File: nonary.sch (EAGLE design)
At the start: 47 parts, among them J1 USB-C-12401598E4#2A, K1 KEYSWITCH-LEDTHTHOLE-MXHS-1U-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, K10 KEYSWITCH-LEDTHTHOLE-MXHS-1U-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, K11 KEYSWITCH-LEDTHTHOLE-MXHS-1U-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, K12 KEYSWITCH-LEDTHTHOLE-MXHS-1U-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, K13 KEYSWITCH-LEDTHTHOLE-MXHS-1U-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, K14 KEYSWITCH-LEDTHTHOLE-MXHS-1U-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, K15 KEYSWITCH-LEDTHTHOLE-MXHS-1U-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, K16 KEYSWITCH-LEDTHTHOLE-MXHS-1U-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, K2 KEYSWITCH-LEDTHTHOLE-MXHS-1U-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, K3 KEYSWITCH-LEDTHTHOLE-MXHS-1U-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, K4 KEYSWITCH-LEDTHTHOLE-MXHS-1U-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, K5 KEYSWITCH-LEDTHTHOLE-MXHS-1U-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, K6 KEYSWITCH-LEDTHTHOLE-MXHS-1U-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, K7 KEYSWITCH-LEDTHTHOLE-MXHS-1U-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, K8 KEYSWITCH-LEDTHTHOLE-MXHS-1U-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, K9 KEYSWITCH-LEDTHTHOLE-MXHS-1U-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

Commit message: updated file names
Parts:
- removed K1, K10, K11, K12, K13, K14, K15, K16, K2, K3, K4, K5, K6, K7, K8, K9: KEYSWITCH-LEDTHTHOLE-MXHS-1U-LEDTHTHOLE, Keyboard:KEYSWITCH-LEDTHTHOLE-MXHS-1U-LEDTHTHOLE
- added D15, D16, D17, D18, D19, D20, D21, D22, D23, D24, D25, D26, D28, D29, D30, D31, D32, D33, D34, D35, D36, D37, D38, D39, D40, D41, D42, D43, D44, D45, D46, D47, D48, D49, D50, D51, D52, D53, D54, D55, D56, D57, D58, D59, D60, D61, D62: (no value), Components:DIODE-DFN0603-2
- added F1, F2, F3, F4, F5, K_", K_,, K_-, K_., K_/, K_0, K_1, K_2, K_3, K_4, K_5, K_6, K_7, K_8, K_9, K_=, K_A, K_B, K_BACKSLASH, K_BACKSPACE, K_C, K_CAPSLOCK, K_D, K_E, K_ENTER, K_F, K_G, K_H, K_I, K_J, K_K, K_L, K_LALT, K_LCTRL, K_LSHIFT, K_LWIN, K_M, K_N, K_O, K_P, K_Q, K_R, K_RALT, K_RCTRL, K_RFN1, K_RFN2, K_RSHIFT, K_RWIN, K_S, K_SEMICOLON, K_SPACE, K_T, K_TAB, K_U, K_V, K_W, K_X, K_Y, K_Z, K_[, K_], K_`: KEYSWITCH-LEDTHTHOLE-MXHS-1U-LEDTHTHOLE, Keyboard:KEYSWITCH-LEDTHTHOLE-MXHS-1U-LEDTHTHOLE
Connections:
- new net COL10: K_..P0, K_9.P0, K_L.P0, K_O.P0, K_RALT.P0
- new net COL12: K_/.P0, K_0.P0, K_P.P0, K_RWIN.P0, K_SEMICOLON.P0
- new net COL13: K_".P0, K_-.P0, K_RFN2.P0, K_RSHIFT.P0, K_[.P0
- new net COL14: K_BACKSLASH.P0, K_BACKSPACE.P0, K_ENTER.P0, K_RCTRL.P0, K_RFN1.P0
- new net COL2: K_1.P0, K_A.P0, K_LWIN.P0, K_Q.P0, K_Z.P0
- new net COL3: K_2.P0, K_LALT.P0, K_S.P0, K_W.P0, K_X.P0
- new net COL4: K_3.P0, K_C.P0, K_D.P0, K_E.P0
- new net COL5: K_4.P0, K_F.P0, K_R.P0, K_V.P0
- new net COL6: K_5.P0, K_B.P0, K_G.P0, K_SPACE.P0, K_T.P0
- new net COL7: K_6.P0, K_H.P0, K_N.P0, K_Y.P0
- new net COL8: K_7.P0, K_J.P0, K_M.P0, K_U.P0
- new net COL9: K_,.P0, K_8.P0, K_I.P0, K_K.P0
- new net N$19: D10.A, D9.C, K_8.P1
- new net N$25: D14.C, K_BACKSPACE.P1
- new net N$26: D15.C, D16.A, K_TAB.P1
- new net N$27: D16.C, D17.A, K_Q.P1
- new net N$28: D17.C, D18.A, K_W.P1
- new net N$29: D18.C, D19.A, K_E.P1
- new net N$30: D19.C, D20.A, K_R.P1
- new net N$31: D20.C, D21.A, K_T.P1
- new net N$32: D21.C, D22.A, K_Y.P1
- new net N$33: D22.C, D23.A, K_U.P1
- new net N$34: D23.C, D24.A, K_I.P1
- new net N$35: D24.C, D25.A, K_O.P1
- new net N$36: D25.C, D26.A, K_P.P1
- new net N$37: D26.C, D27.A, K_[.P1
- new net N$38: D34.C, D35.A, K_G.P1
- new net N$39: D27.C, D28.A, K_].P1
- new net N$40: D41.C, K_ENTER.P1
- new net N$41: D29.C, D30.A, K_CAPSLOCK.P1
- new net N$42: D30.C, D31.A, K_A.P1
- new net N$43: D31.C, D32.A, K_S.P1
- new net N$44: D32.C, D33.A, K_D.P1
- new net N$45: D33.C, D34.A, K_F.P1
- new net N$46: D40.C, D41.A, K_".P1
- new net N$47: D35.C, D36.A, K_H.P1
- new net N$48: D36.C, D37.A, K_J.P1
- new net N$49: D37.C, D38.A, K_K.P1
- new net N$50: D38.C, D39.A, K_L.P1
- new net N$51: D39.C, D40.A, K_SEMICOLON.P1
- new net N$52: D53.C, D54.A, K_RSHIFT.P1
- new net N$53: D54.C, K_RFN1.P1
- new net N$54: D47.C, D48.A, K_B.P1
- new net N$55: D60.C, D61.A, K_RWIN.P1
- new net N$56: D42.C, D43.A, K_LSHIFT.P1
- new net N$57: D43.C, D44.A, K_Z.P1
- new net N$58: D44.C, D45.A, K_X.P1
- new net N$59: D45.C, D46.A, K_C.P1
- new net N$60: D46.C, D47.A, K_V.P1
- new net N$61: K_=.P0, K_].P0
- new net N$62: D48.C, D49.A, K_N.P1
- new net N$63: D49.C, D50.A, K_M.P1
- new net N$64: D50.C, D51.A, K_,.P1
- new net N$65: D51.C, D52.A, K_..P1
- new net N$66: D52.C, D53.A, K_/.P1
- new net N$71: D55.C, D56.A, K_LCTRL.P1
- new net N$72: D56.C, D57.A, K_LWIN.P1
- new net N$73: D57.C, D58.A, K_LALT.P1
- new net N$74: D58.C, D59.A, K_SPACE.P1
- new net N$75: D59.C, D60.A, K_RALT.P1
- new net N$77: D61.C, D62.A, K_RFN2.P1
- new net N$78: D62.C, K_RCTRL.P1
- new net ROW1: D15.A, F2.P1, U$1.PF1(ADC1)
- new net ROW3: D42.A, F4.P1, U$1.PF5(ADC5)
- new net ROW4: D55.A, F5.P1, U$1.PF6(ADC6)
- net COL0: now also F1.P0, F2.P0, F3.P0, F4.P0, F5.P0, U$1.PF7(ADC7); no longer K1.P0, K15.P0, K16.P0, U$1.PF4(ADC4)
- net COL1: now also K_CAPSLOCK.P0, K_LCTRL.P0, K_LSHIFT.P0, K_TAB.P0, K_`.P0; no longer U$1.PF5(ADC5)
- net N$11: now also D1.C, D2.A, K_`.P1; no longer D2.C, D3.A, K3.P1
- net N$12: now also D2.C, D3.A, K_1.P1; no longer D3.C, D4.A, K4.P1
- net N$13: now also D3.C, D4.A, K_2.P1; no longer D1.C, D2.A, K2.P1
- net N$14: now also K_3.P1; no longer K5.P1
- net N$15: now also K_4.P1; no longer K6.P1
- net N$16: now also K_5.P1; no longer K7.P1
- net N$17: now also K_6.P1; no longer K8.P1
- net N$18: now also K_7.P1; no longer K9.P1
- net N$20: now also D10.C, D11.A, K_9.P1; no longer D10.A, D9.C, K10.P1
- net N$21: now also D11.C, D12.A, K_0.P1; no longer D10.C, D11.A, K11.P1
- net N$22: now also D12.C, D13.A, K_-.P1; no longer D11.C, D12.A, K12.P1
- net N$23: now also D28.C, K_BACKSLASH.P1; no longer D12.C, D13.A, K13.P1
- net N$24: now also D14.A, K_=.P1; no longer K14.P1
- net N$7: now also R3.1; no longer R3.2
- net N$8: now also R3.2; no longer R3.1
- net ROW0: now also F1.P1; no longer K1.P1
- net ROW2: now also D29.A, F3.P1, U$1.PF4(ADC4); no longer D14.A, D27.A, K15.P1, K16.P1, U$1.PF1(ADC1)
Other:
- note added: "Fn Keys"
- note removed: "Power"
- moved on the sheet: C1, C2, C3, C4, C5, C6, C7, C8, D1, D10, D11, D12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

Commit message: Made modifications to the keyboard.lbr, brd, and sch files
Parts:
- removed D1, D10, D11, D12, D13, D14, D15, D16, D17, D18, D19, D2, D20, D21, D22, D23, D24, D25, D26, D27, D28, D29, D3, D30, D31, D32, D33, D34, D35, D36, D37, D38, D39, D4, D40, D41, D42, D43, D44, D45, D46, D47, D48, D49, D5, D50, D51, D52, D53, D54, D55, D56, D57, D58, D59, D6, D60, D61, D62, D8, D9: (no value), Components:DIODE-DFN0603-2
- removed F1, F3, F4, F5, K_", K_,, K_-, K_., K_/, K_0, K_1, K_2, K_3, K_4, K_5, K_6, K_7, K_8, K_9, K_=, K_A, K_B, K_BACKSLASH, K_BACKSPACE, K_C, K_CAPSLOCK, K_D, K_E, K_ENTER, K_F, K_G, K_H, K_I, K_J, K_K, K_L, K_LALT, K_LCTRL, K_LSHIFT, K_LWIN, K_M, K_N, K_O, K_P, K_Q, K_R, K_RALT, K_RCTRL, K_RFN1, K_RFN2, K_RSHIFT, K_RWIN, K_S, K_SEMICOLON, K_SPACE, K_T, K_TAB, K_U, K_V, K_W, K_X, K_Y, K_Z, K_[, K_], K_`: KEYSWITCH-LEDTHTHOLE-MXHS-1U-LEDTHTHOLE, Keyboard:KEYSWITCH-LEDTHTHOLE-MXHS-1U-LEDTHTHOLE
- removed J1: USB-C-12401598E4#2A, USB:USB-C-12401598E4#2A
- removed R4: 22, rcl:R-US_R0603
- added C10, C11, C9: 0.1uF, Components:CAPACITOR-0603
- added C12, C13, C14: 0.47uF, Components:CAPACITOR-0603
- added IC1: IS31FL3733-TQLS4, SamacSys_Parts:IS31FL3733-TQLS4
- added IC2: TLV75533PDBVR, SamacSys_Parts:TLV75533PDBVR
- added J2: USB4065-XX-X_REVA, USB4065-XX-X_REVA:USB4065-XX-X_REVA
- added K1, K2, K3, K4, K5, K6, K7, K8, K9: KEYSWITCH-RGBSMDLED-MXHSPCB-1U-SMDRGB, Keyboard:KEYSWITCH-RGBSMDLED-MXHSPCB-1U-SMDRGB
- added Q1, Q2: BSS138, SamacSys_Parts:BSS138
- added R10, R11, R8, R9: 10K, rcl:R-US_R0603
- added R5, R6: 5.1k, rcl:R-US_R0603
- added SV1: (no value), con-lstb:MA04-1
- C8: value 22pF -> 1uF
- D7: value (none) -> PRTR5V0U2X,215; device Components:DIODE-DFN0603-2 -> SamacSys_Parts:PRTR5V0U2X,215
- F2: value KEYSWITCH-LEDTHTHOLE-MXHS-1U-LEDTHTHOLE -> MF-PSMF020X-2; device Keyboard:KEYSWITCH-LEDTHTHOLE-MXHS-1U-LEDTHTHOLE -> SamacSys_Parts:MF-PSMF020X-2
- R3: value 22 -> 10K
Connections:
- net N$1 renamed XTAL1
- net N$2 renamed XTAL2
- removed net COL0: F1.P0, F2.P0, F3.P0, F4.P0, F5.P0, U$1.PF7(ADC7)
- removed net COL1: K_CAPSLOCK.P0, K_LCTRL.P0, K_LSHIFT.P0, K_TAB.P0, K_`.P0
- removed net COL10: K_..P0, K_9.P0, K_L.P0, K_O.P0, K_RALT.P0
- removed net COL12: K_/.P0, K_0.P0, K_P.P0, K_RWIN.P0, K_SEMICOLON.P0
- removed net COL13: K_".P0, K_-.P0, K_RFN2.P0, K_RSHIFT.P0, K_[.P0
- removed net COL14: K_BACKSLASH.P0, K_BACKSPACE.P0, K_ENTER.P0, K_RCTRL.P0, K_RFN1.P0
- removed net COL2: K_1.P0, K_A.P0, K_LWIN.P0, K_Q.P0, K_Z.P0
- removed net COL3: K_2.P0, K_LALT.P0, K_S.P0, K_W.P0, K_X.P0
- removed net COL4: K_3.P0, K_C.P0, K_D.P0, K_E.P0
- removed net COL5: K_4.P0, K_F.P0, K_R.P0, K_V.P0
- removed net COL6: K_5.P0, K_B.P0, K_G.P0, K_SPACE.P0, K_T.P0
- removed net COL7: K_6.P0, K_H.P0, K_N.P0, K_Y.P0
- removed net COL8: K_7.P0, K_J.P0, K_M.P0, K_U.P0
- removed net COL9: K_,.P0, K_8.P0, K_I.P0, K_K.P0
- removed net N$10: J1.D_M, R4.2
- removed net N$11: D1.C, D2.A, K_`.P1
- removed net N$12: D2.C, D3.A, K_1.P1
- removed net N$14: D4.C, D5.A, K_3.P1
- removed net N$15: D5.C, D6.A, K_4.P1
- removed net N$16: D6.C, D7.A, K_5.P1
- removed net N$17: D7.C, D8.A, K_6.P1
- removed net N$18: D8.C, D9.A, K_7.P1
- removed net N$20: D10.C, D11.A, K_9.P1
- removed net N$21: D11.C, D12.A, K_0.P1
- removed net N$22: D12.C, D13.A, K_-.P1
- removed net N$23: D28.C, K_BACKSLASH.P1
- removed net N$24: D13.C, D14.A, K_=.P1
- removed net N$25: D14.C, K_BACKSPACE.P1
- removed net N$28: D17.C, D18.A, K_W.P1
- removed net N$29: D18.C, D19.A, K_E.P1
- removed net N$30: D19.C, D20.A, K_R.P1
- removed net N$31: D20.C, D21.A, K_T.P1
- removed net N$32: D21.C, D22.A, K_Y.P1
- removed net N$33: D22.C, D23.A, K_U.P1
- removed net N$34: D23.C, D24.A, K_I.P1
- removed net N$35: D24.C, D25.A, K_O.P1
- removed net N$36: D25.C, D26.A, K_P.P1
- removed net N$37: D26.C, D27.A, K_[.P1
- removed net N$38: D34.C, D35.A, K_G.P1
- removed net N$39: D27.C, D28.A, K_].P1
- removed net N$40: D41.C, K_ENTER.P1
- removed net N$41: D29.C, D30.A, K_CAPSLOCK.P1
- removed net N$42: D30.C, D31.A, K_A.P1
- removed net N$43: D31.C, D32.A, K_S.P1
- removed net N$44: D32.C, D33.A, K_D.P1
- removed net N$45: D33.C, D34.A, K_F.P1
- removed net N$46: D40.C, D41.A, K_".P1
- removed net N$47: D35.C, D36.A, K_H.P1
- removed net N$48: D36.C, D37.A, K_J.P1
- removed net N$49: D37.C, D38.A, K_K.P1
- removed net N$50: D38.C, D39.A, K_L.P1
- removed net N$51: D39.C, D40.A, K_SEMICOLON.P1
- removed net N$52: D53.C, D54.A, K_RSHIFT.P1
- removed net N$53: D54.C, K_RFN1.P1
- removed net N$54: D47.C, D48.A, K_B.P1
- removed net N$55: D60.C, D61.A, K_RWIN.P1
- removed net N$56: D42.C, D43.A, K_LSHIFT.P1
- removed net N$57: D43.C, D44.A, K_Z.P1
- removed net N$58: D44.C, D45.A, K_X.P1
- removed net N$59: D45.C, D46.A, K_C.P1
- removed net N$6: J1.VCC, U$1.UVCC
- removed net N$60: D46.C, D47.A, K_V.P1
- removed net N$61: K_=.P0, K_].P0
- removed net N$62: D48.C, D49.A, K_N.P1
- removed net N$63: D49.C, D50.A, K_M.P1
- removed net N$64: D50.C, D51.A, K_,.P1
- removed net N$65: D51.C, D52.A, K_..P1
- removed net N$66: D52.C, D53.A, K_/.P1
- removed net N$7: J1.D_P, R3.1
- removed net N$71: D55.C, D56.A, K_LCTRL.P1
- removed net N$72: D56.C, D57.A, K_LWIN.P1
- removed net N$73: D57.C, D58.A, K_LALT.P1
- removed net N$74: D58.C, D59.A, K_SPACE.P1
- removed net N$75: D59.C, D60.A, K_RALT.P1
- removed net N$77: D61.C, D62.A, K_RFN2.P1
- removed net N$78: D62.C, K_RCTRL.P1
- removed net N$8: R3.2, U$1.D+
- removed net N$9: R4.1, U$1.D-
- removed net ROW0: D1.A, F1.P1, U$1.PF0(ADC0)
- removed net ROW1: D15.A, F2.P1, U$1.PF1(ADC1)
- removed net ROW2: D29.A, F3.P1, U$1.PF4(ADC4)
- removed net ROW3: D42.A, F4.P1, U$1.PF5(ADC5)
- removed net ROW4: D55.A, F5.P1, U$1.PF6(ADC6)
- removed net VCC: C3.2, C4.2, C5.2, C6.2, C7.2, U$1.AVCC@24, U$1.AVCC@44, U$1.VBUS, U$1.VCC@14, U$1.VCC@34
- new net +5V: C3.2, C4.2, C5.2, C6.2, C7.2, F2.1, IC2.EN, IC2.IN, R1.1, R10.1, R8.1, SV1.3, U$1.AVCC@24, U$1.AVCC@44, U$1.UVCC, U$1.VBUS, U$1.VCC@14, U$1.VCC@34
- new net AVCC: C12.2, C9.2, IC1.AVCC, IC1.DVCC
- new net CS1: IC1.CS3, K3.LED+, K6.LED+, K9.LED+
- new net CS2: IC1.CS2, K2.LED+, K5.LED+, K8.LED+
- new net CS3: IC1.CS1, K1.LED+, K4.LED+, K7.LED+
- new net D+: D7.I/O_1, J2.DP1, J2.DP2, U$1.D+
- new net D-: D7.I/O_2, J2.DN1, J2.DN2, U$1.D-
- new net KEY1: K1.P0, U$1.PD7(ADC10)
- new net KEY2: K2.P0, U$1.PF5(ADC5)
- new net KEY3: K3.P0, U$1.PF0(ADC0)
- new net KEY4: K4.P0, U$1.PD6(ADC9)
- new net KEY5: K5.P0, U$1.PF6(ADC6)
- new net KEY6: K6.P0, U$1.PF1(ADC1)
- new net KEY7: K7.P0, U$1.PD4(ADC8)
- new net KEY8: K8.P0, U$1.PF7(ADC7)
- new net KEY9: K9.P0, U$1.PF4(ADC4)
- new net PVCC_1: C11.2, C14.2, IC1.PVCC_1
- new net PVCC_2: C10.2, C13.2, IC1.PVCC_2
- new net SCL: Q2.D, R10.2, U$1.PD0(SCL)
- new net SCL_3V3: IC1.SCL, Q2.S, R11.2, SV1.2
- new net SDA: Q1.D, R8.2, U$1.PD1(SDA)
- new net SDA_3V3: IC1.SDA, Q1.S, R9.2, SV1.1
- new net SW1: IC1.SW1, K1.B-, K2.B-, K3.B-
- new net SW2: IC1.SW2, K1.G-, K2.G-, K3.G-
- new net SW3: IC1.SW3, K1.R-, K2.R-, K3.R-
- new net SW4: IC1.SW4, K4.B-, K5.B-, K6.B-
- new net SW5: IC1.SW5, K4.G-, K5.G-, K6.G-
- new net SW6: IC1.SW6, K4.R-, K5.R-, K6.R-
- new net SW7: IC1.SW7, K7.B-, K8.B-, K9.B-
- new net SW8: IC1.SW8, K7.G-, K8.G-, K9.G-
- new net SW9: IC1.SW9, K7.R-, K8.R-, K9.R-
- net +3V3: now also IC1.VIO, IC2.OUT, Q1.G, Q2.G, R11.1, R9.1; no longer R1.1
- net GND: now also C10.1, C11.1, C12.1, C13.1, C14.1, C9.1, D7.GND, IC1.ADDR1, IC1.ADDR2, IC1.AGND, IC1.GND_1, IC1.GND_2, IC1.PGND_1, IC1.PGND_2, IC2.GND, IC2.NC, J2.GND1.1, J2.GND1.2, J2.GND2.1, J2.GND2.2, J2.SHIELD, K1.P1, K2.P1, K3.P1, K4.P1, K5.P1, K6.P1, K7.P1, K8.P1, K9.P1, R3.2, R5.2, R6.2, SV1.4; no longer J1.GND, J1.SHIELD
- net N$13: now also J2.CC2, R5.1; no longer D3.C, D4.A, K_2.P1
- net N$19: now also J2.CC1, R6.1; no longer D10.A, D9.C, K_8.P1
- net N$26: now also IC1.RSET, R3.1; no longer D15.C, D16.A, K_TAB.P1
- net N$27: now also D7.VCC, F2.2, J2.VBUS1.1, J2.VBUS2.2; no longer D16.C, D17.A, K_Q.P1
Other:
- note added: "Switch Matrix"
- note added: "USB Type-C"
- note removed: "Fn Keys"
- note removed: "USB"
- moved on the sheet: C1, C2, C3, C4, C5, C6, C7, C8, R1, R2, R3, S1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

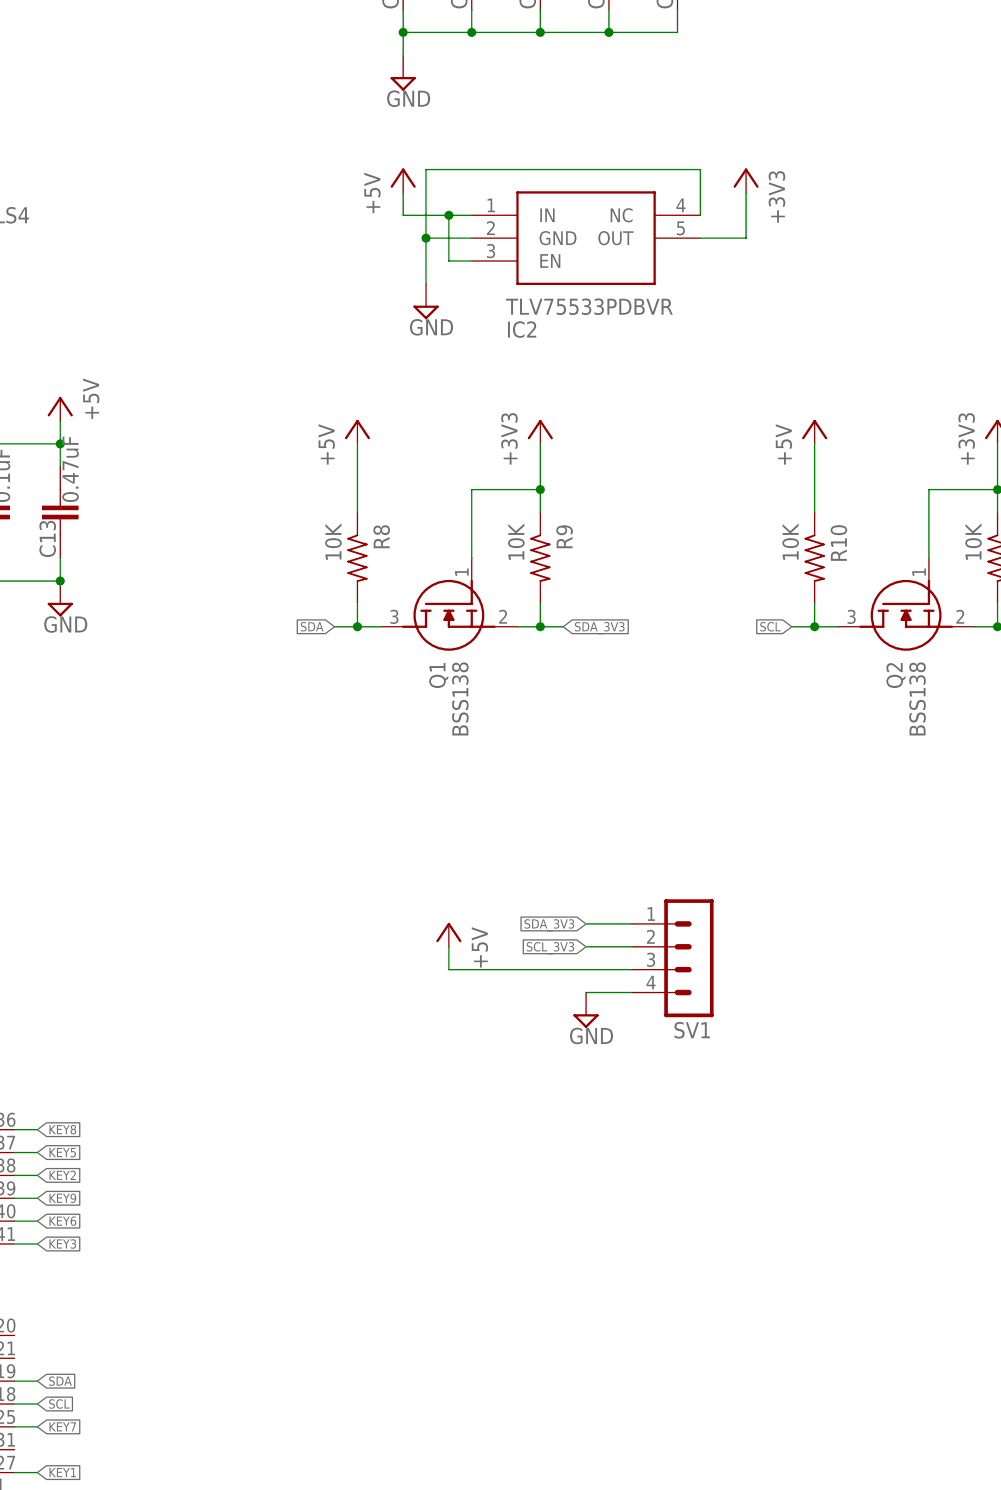
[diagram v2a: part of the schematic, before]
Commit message: Routing on the Board
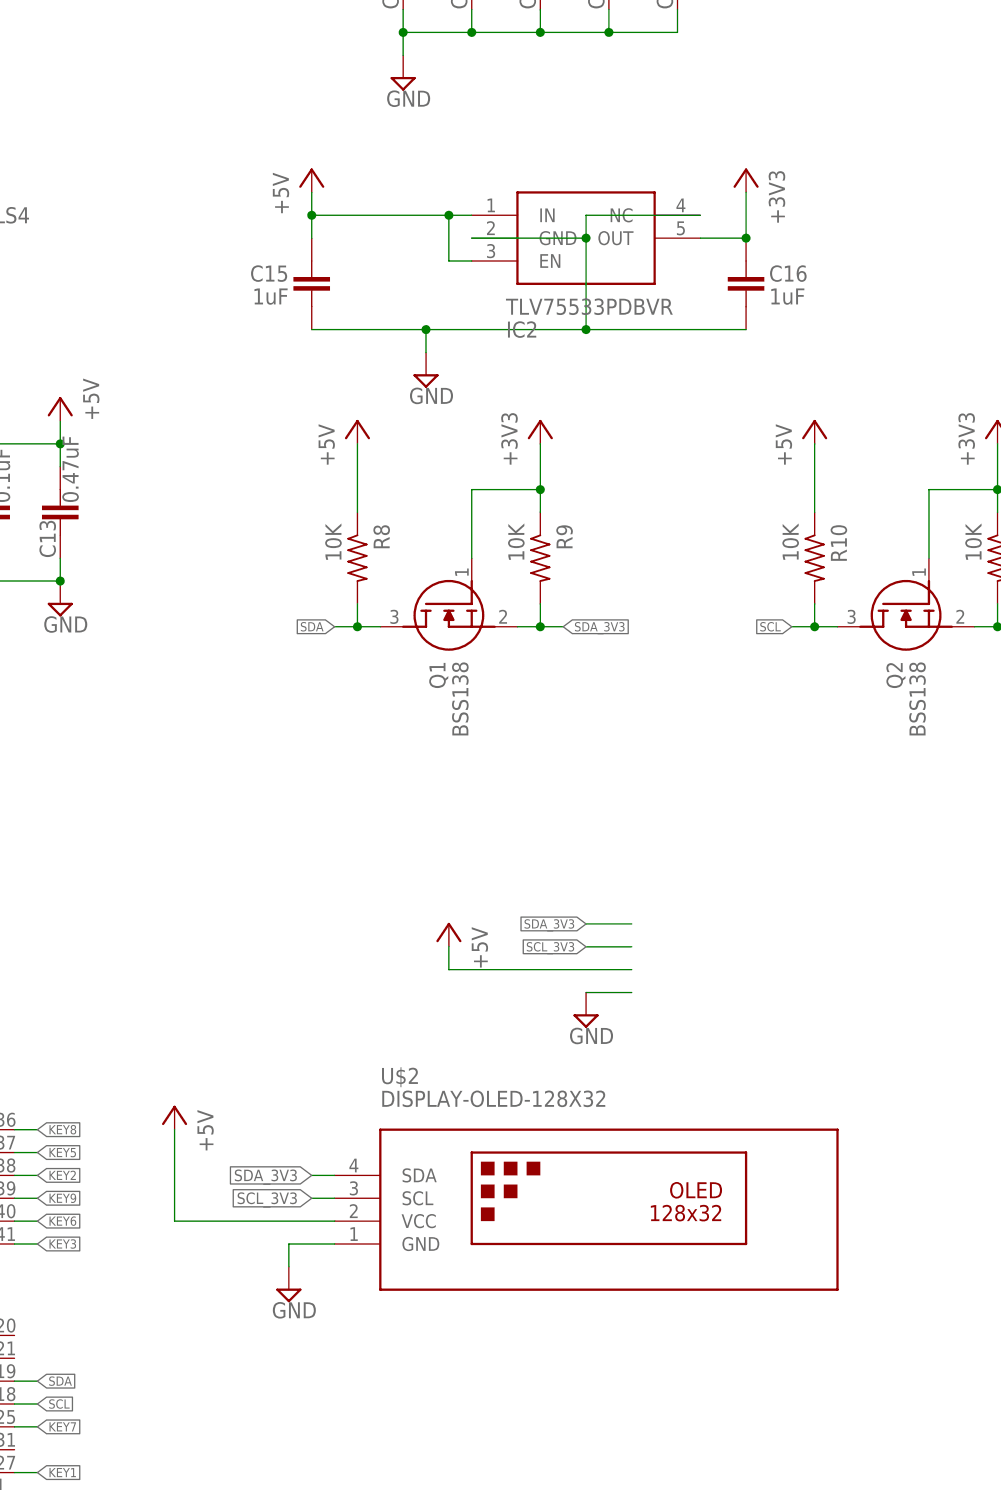
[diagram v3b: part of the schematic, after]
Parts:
- removed SV1: (no value), con-lstb:MA04-1
- added C15, C16: 1uF, Components:CAPACITOR-0603
- added U$2: DISPLAY-OLED-128X32, diy-modules:DISPLAY-OLED-128X32
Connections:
- net N$3 renamed /RESET
- net +3V3: now also C16.2
- net +5V: now also C15.2, U$2.VCC; no longer SV1.3
- net GND: now also C15.1, C16.1, U$2.GND; no longer SV1.4
- net SCL_3V3: now also U$2.SCL; no longer SV1.2
- net SDA_3V3: now also U$2.SDA; no longer SV1.1

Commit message: New Libraries and finished board/schematic
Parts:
- removed IC2: TLV75533PDBVR, SamacSys_Parts:TLV75533PDBVR
- removed U$1: ATMEGA32U4TQFP, SparkFun-Retired:ATMEGA32U4TQFP
- removed U$2: DISPLAY-OLED-128X32, diy-modules:DISPLAY-OLED-128X32
- added C17: 1uF, Components:CAPACITOR-0603
- added R12, R13: 100K, rcl:R-US_R0603
- added R4, R7: 4.7k, rcl:R-US_R0603
- added U1: ATMEGA32U4TQFP, SparkFun-Retired:ATMEGA32U4TQFP
- added U2: (no value), LED:IS31FL3737
- added U3: DISPLAY-OLED-128X32, diy-modules:DISPLAY-OLED-128X32
- C12: value 0.47uF -> 0.1uF
- C15: value 1uF -> 0.47uF
- C9: value 0.1uF -> 0.47uF
- IC1: value IS31FL3733-TQLS4 -> TLV75533PDBVR; device SamacSys_Parts:IS31FL3733-TQLS4 -> SamacSys_Parts:TLV75533PDBVR
- J2: value USB4065-XX-X_REVA -> USB-C-12401598E4#2A; device USB4065-XX-X_REVA:USB4065-XX-X_REVA -> USB:USB-C-12401598E4#2A
- R3: value 10K -> 20K
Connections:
- removed net AVCC: C12.2, C9.2, IC1.AVCC, IC1.DVCC
- removed net N$19: J2.CC1, R6.1
- removed net N$26: IC1.RSET, R3.1
- removed net PVCC_1: C11.2, C14.2, IC1.PVCC_1
- removed net PVCC_2: C10.2, C13.2, IC1.PVCC_2
- new net N$1: R12.1, U2.IICRST
- new net N$2: R3.1, U2.RSET
- new net N$3: J2.CC, R6.1
- new net SDB: R13.1, U1.PE6, U2.SDB
- net +3V3: now also C17.2, C9.1, IC1.OUT, R4.1, R7.1, U2.VIO; no longer C16.2, IC1.VIO, IC2.OUT
- net +5V: now also C10.2, C11.2, C12.2, C13.2, C14.2, C16.2, IC1.EN, IC1.IN, U1.AREF, U1.AVCC@24, U1.AVCC@44, U1.UVCC, U1.VBUS, U1.VCC@14, U1.VCC@34, U2.PVCC1, U2.PVCC2, U2.VCC, U3.VCC; no longer IC2.EN, IC2.IN, U$1.AVCC@24, U$1.AVCC@44, U$1.UVCC, U$1.VBUS, U$1.VCC@14, U$1.VCC@34, U$2.VCC
- net /RESET: now also U1.!RESET; no longer U$1.!RESET
- net CS1: now also U2.CS1; no longer IC1.CS3
- net CS2: now also U2.CS2; no longer IC1.CS2
- net CS3: now also U2.CS3; no longer IC1.CS1
- net D+: now also J2.D_P, U1.D+; no longer J2.DP1, J2.DP2, U$1.D+
- net D-: now also J2.D_M, U1.D-; no longer J2.DN1, J2.DN2, U$1.D-
- net GND: now also C17.1, C9.2, IC1.GND, J2.GND, R12.2, R13.2, U1.GND@15, U1.GND@23, U1.GND@35, U1.GND@43, U1.UGND, U2.ADDR, U2.AGND, U2.GND, U2.PGND1, U2.PGND2, U3.GND; no longer C9.1, IC1.ADDR1, IC1.ADDR2, IC1.AGND, IC1.GND_1, IC1.GND_2, IC1.PGND_1, IC1.PGND_2, IC2.GND, IC2.NC, J2.GND1.1, J2.GND1.2, J2.GND2.1, J2.GND2.2, U$1.GND@15, U$1.GND@23, U$1.GND@35, U$1.GND@43, U$1.UGND, U$2.GND
- net KEY1: now also U1.PD7(ADC10); no longer U$1.PD7(ADC10)
- net KEY2: now also U1.PF5(ADC5); no longer U$1.PF5(ADC5)
- net KEY3: now also U1.PF0(ADC0); no longer U$1.PF0(ADC0)
- net KEY4: now also U1.PD6(ADC9); no longer U$1.PD6(ADC9)
- net KEY5: now also U1.PF6(ADC6); no longer U$1.PF6(ADC6)
- net KEY6: now also U1.PF1(ADC1); no longer U$1.PF1(ADC1)
- net KEY7: now also U1.PD4(ADC8); no longer U$1.PD4(ADC8)
- net KEY8: now also U1.PF7(ADC7); no longer U$1.PF7(ADC7)
- net KEY9: now also U1.PF4(ADC4); no longer U$1.PF4(ADC4)
- net N$27: now also J2.VCC; no longer J2.VBUS1.1, J2.VBUS2.2
- net N$4: now also U1.PE2/!HWB; no longer U$1.PE2/!HWB
- net N$5: now also U1.UCAP; no longer U$1.UCAP
- net SCL: now also U1.PD0(SCL); no longer U$1.PD0(SCL)
- net SCL_3V3: now also R7.2, U2.SCL, U3.SCL; no longer IC1.SCL, U$2.SCL
- net SDA: now also U1.PD1(SDA); no longer U$1.PD1(SDA)
- net SDA_3V3: now also R4.2, U2.SDA, U3.SDA; no longer IC1.SDA, U$2.SDA
- net SW1: now also U2.SW1; no longer IC1.SW1
- net SW2: now also U2.SW2; no longer IC1.SW2
- net SW3: now also U2.SW3; no longer IC1.SW3
- net SW4: now also U2.SW4; no longer IC1.SW4
- net SW5: now also U2.SW5; no longer IC1.SW5
- net SW6: now also U2.SW6; no longer IC1.SW6
- net SW7: now also U2.SW7; no longer IC1.SW7
- net SW8: now also U2.SW8; no longer IC1.SW8
- net SW9: now also U2.SW9; no longer IC1.SW9
- net XTAL1: now also U1.XTAL1; no longer U$1.XTAL1
- net XTAL2: now also U1.XTAL2; no longer U$1.XTAL2
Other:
- moved on the sheet: C1, C10, C11, C12, C13, C14, C15, C16, C2, C3, C4, C5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
